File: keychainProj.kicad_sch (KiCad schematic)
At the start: 0 parts

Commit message: Getting the essential MCUs and accelerometer
Added some choices for the MCU and a potential accelerometer
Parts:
- added BT1: Battery_Cell, symbol Device:Battery_Cell
- added BZ1: Buzzer, symbol Device:Buzzer
- added U1: ATtiny85V-10P, Package_DIP:DIP-8_W7.62mm, symbol MCU_Microchip_ATtiny:ATtiny85V-10P
- added U2: LIS3DH, Package_LGA:LGA-16_3x3mm_P0.5mm_LayoutBorder3x5y, symbol Sensor_Motion:LIS3DH
- added U3: ATtiny1616-S, Package_SO:SOIC-20W_7.5x12.8mm_P1.27mm, symbol MCU_Microchip_ATtiny:ATtiny1616-S
- added U4: CH32V003FxPx, Package_SO:TSSOP-20_4.4x6.5mm_P0.65mm, symbol MCU_WCH_RiscV:CH32V003FxPx
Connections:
- new net: U2.10 (GND), U2.12 (GND), U2.5 (GND)
- new net 3.3V: BT1.1 (+)
- no-connect marks 0 -> 3

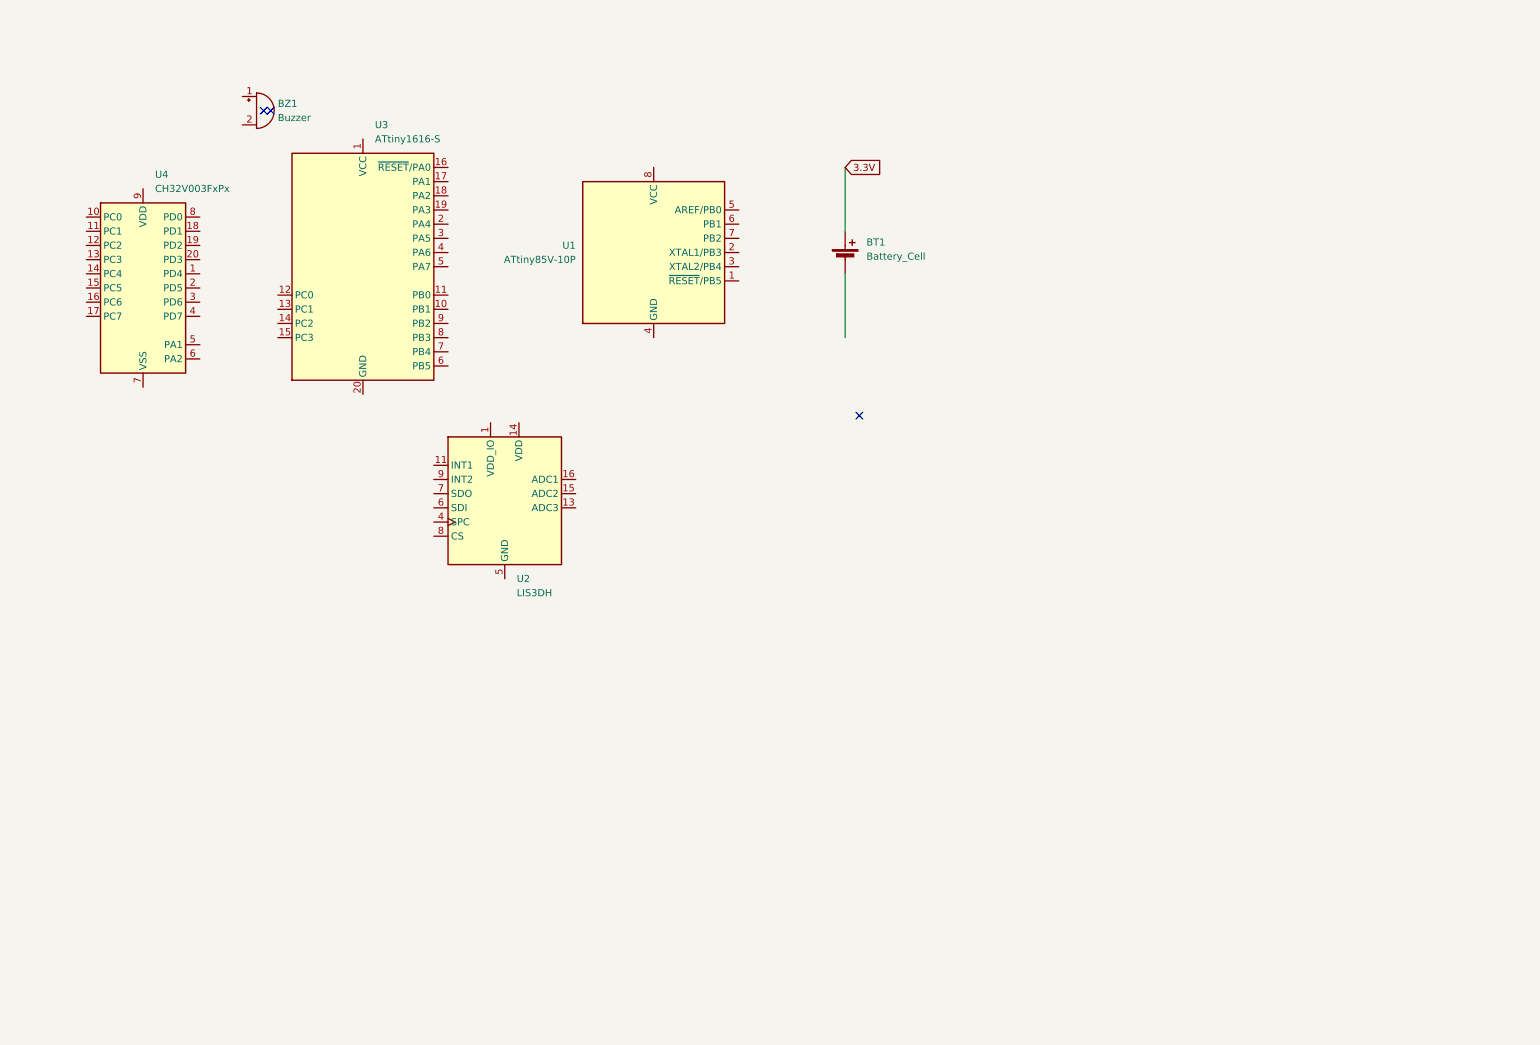
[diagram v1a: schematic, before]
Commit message: Connected the traces and put silkscreen on the PCB
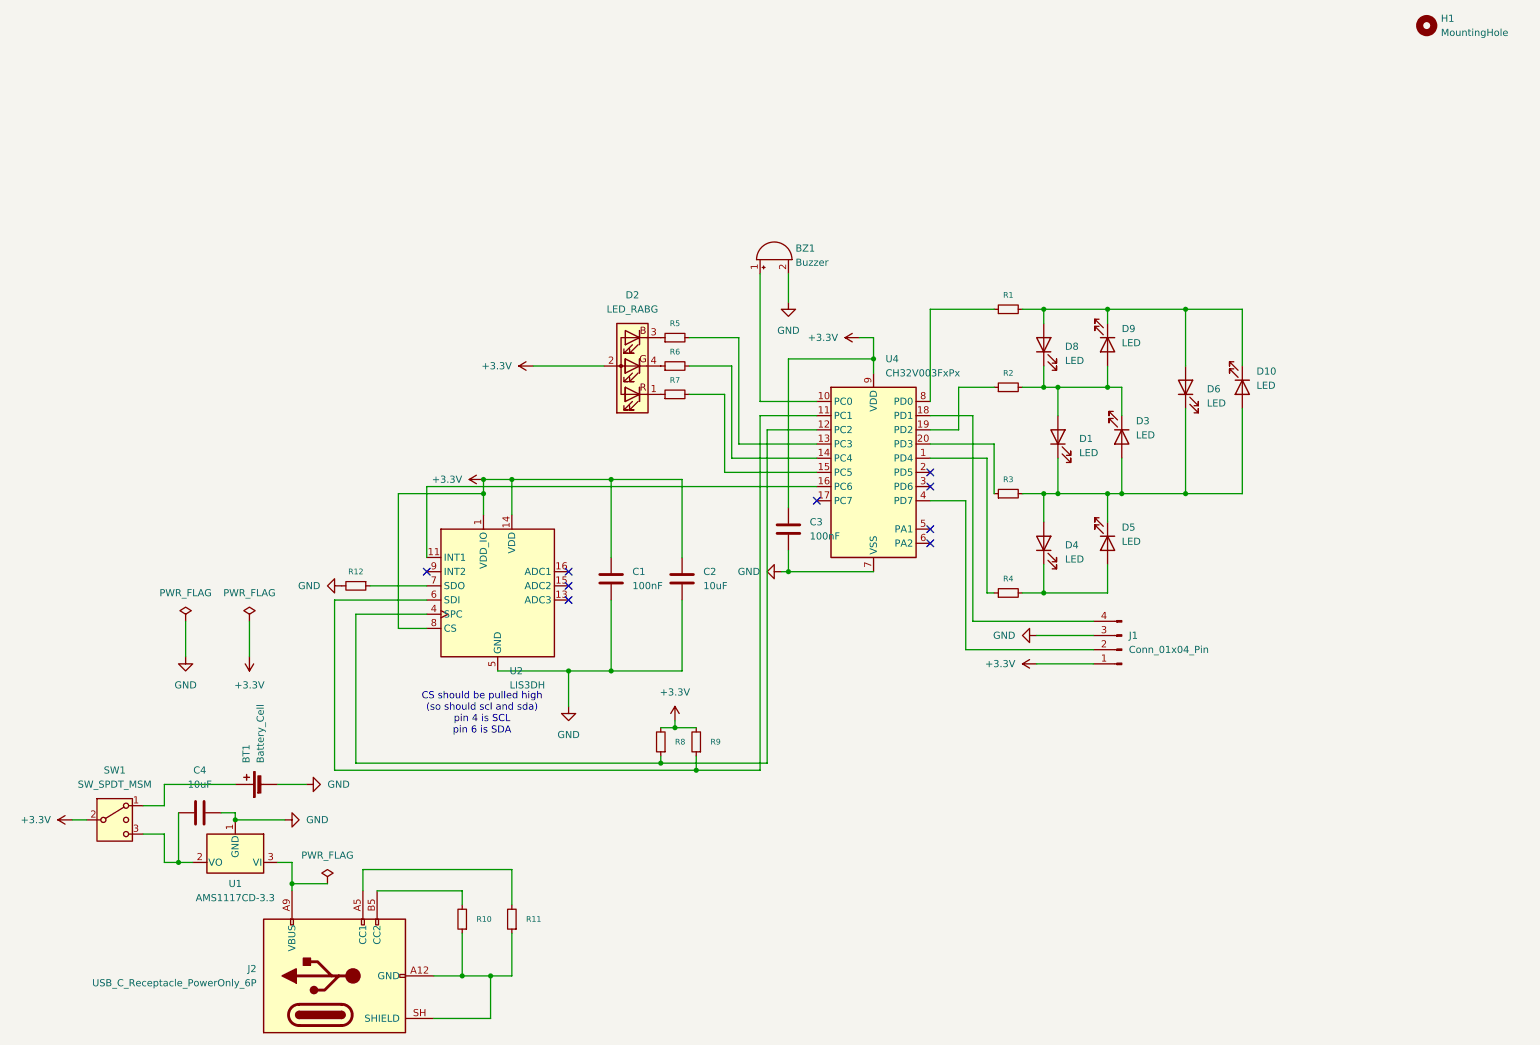
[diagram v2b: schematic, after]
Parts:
- removed U1: ATtiny85V-10P, Package_DIP:DIP-8_W7.62mm, symbol MCU_Microchip_ATtiny:ATtiny85V-10P
- removed U3: ATtiny1616-S, Package_SO:SOIC-20W_7.5x12.8mm_P1.27mm, symbol MCU_Microchip_ATtiny:ATtiny1616-S
- added C1, C3: 100nF, Capacitor_SMD:C_0805_2012Metric, symbol Device:C
- added C2, C4: 10uF, Capacitor_SMD:C_0805_2012Metric, symbol Device:C
- added D1, D10, D3, D4, D5, D6, D8, D9: LED, LED_SMD:LED_0805_2012Metric, symbol Device:LED
- added D2: LED_RABG, LED_SMD:LED_RGB_1210, symbol Device:LED_RABG
- added H1: MountingHole, MountingHole:MountingHole_3mm, symbol Mechanical:MountingHole
- added J1: Conn_01x04_Pin, Connector_PinHeader_2.54mm:PinHeader_1x04_P2.54mm_Vertical, symbol Connector:Conn_01x04_Pin
- added J2: USB_C_Receptacle_PowerOnly_6P, Connector_USB:USB_C_Receptacle_GCT_USB4085, symbol Connector:USB_C_Receptacle_PowerOnly_6P
- added R1, R2, R3, R4: 100, Resistor_SMD:R_0805_2012Metric, symbol Device:R_Small
- added R10, R11: 5k1, Resistor_SMD:R_0805_2012Metric, symbol Device:R_Small
- added R12, R8, R9: 4k7, Resistor_SMD:R_0805_2012Metric, symbol Device:R_Small
- added R5, R6: 47, Resistor_SMD:R_0805_2012Metric, symbol Device:R_Small
- added R7: 330, Resistor_SMD:R_0805_2012Metric, symbol Device:R_Small
- added SW1: SW_SPDT_MSM, Button_Switch_THT:SW_Slide_SPDT_Straight_CK_OS102011MS2Q, symbol Switch:SW_SPDT_MSM
- added U1: AMS1117CD-3.3, Package_TO_SOT_SMD:TO-252-3_TabPin2, symbol Regulator_Linear:AMS1117CD-3.3
- BT1: footprint (none) -> Battery:BatteryHolder_Keystone_1058_1x2032
- BZ1: footprint (none) -> Buzzer_Beeper:Buzzer_12x9.5RM7.6
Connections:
- net at BZ1.1 (+): now also U4.10 (PC0)
- net GND: now reaches BZ1.2 (-)
- net GND: now also BT1.2 (-), U2.10 (GND), U2.12 (GND), U2.5 (GND), U4.7 (VSS), C1.2, C2.2, C3.2, C4.2, J1.3 (Pin_3), R12.2, U1.1 (GND)
- net at U4.1 (PD4): now also R4.1
- net at U4.11 (PC1): now also U2.6 (SDI), R9.1
- net at U4.12 (PC2): now also U2.4 (SPC), R8.1
- net at U4.13 (PC3): now also R5.2
- net at U4.14 (PC4): now also R6.2
- net at U4.15 (PC5): now also R7.2
- net at U4.16 (PC6): now also U2.11 (INT1)
- net at U4.18 (PD1): now also J1.4 (Pin_4)
- net at U4.19 (PD2): now also R2.1
- net at U4.20 (PD3): now also R3.1
- net at U4.4 (PD7): now also J1.2 (Pin_2)
- net at U4.8 (PD0): now also R1.1
- net +3.3V: now reaches U4.9 (VDD)
- net +3.3V: now also U2.1 (VDD_IO), U2.14 (VDD), U2.8 (CS), C1.1, C2.1, C3.1, D2.2 (A), J1.1 (Pin_1), R8.2, R9.2, SW1.2 (3)
- net at U2.7 (SDO): now also R12.1
- net 3.3V: no longer names the net of BT1.1 (+)
- net 3.3V: now also SW1.1
- new net: D10.1 (K), D6.2 (A), D8.2 (A), D9.1 (K), R1.2
- new net: D1.2 (A), D3.1 (K), D8.1 (K), D9.2 (A), R2.2
- new net: D2.1 (RK), R7.1
- new net: D2.3 (BK), R5.1
- new net: D2.4 (GK), R6.1
- new net: D1.1 (K), D10.2 (A), D3.2 (A), D4.2 (A), D5.1 (K), D6.1 (K), R3.2
- new net: J2.A12 (GND), J2.B12 (GND), J2.SH (SHIELD), R10.1, R11.1
- new net: J2.A5 (CC1), R11.2
- new net: D4.1 (K), D5.2 (A), R4.2
- new net: J2.A9 (VBUS), J2.B9 (VBUS), U1.3 (VI)
- new net: J2.B5 (CC2), R10.2
- new net: C4.1, SW1.3 (4), U1.2 (VO)
- no-connect marks 3 -> 9
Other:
- note added: "CS should be pulled high (so should scl and sda) pin 4 is SCL pin 6 is SDA"
- moved on the sheet: BT1, BZ1, U2, U4
